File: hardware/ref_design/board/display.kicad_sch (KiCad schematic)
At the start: 13 parts, among them J3 FH35C-39S-0.3SHW(50), U6 TPS61160DRVR

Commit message: Reference design: case, board pipeline, routing tools and docs
- case/case.scad now owns every position the board needs (outline,
  cable slot, contacts, screws, USB-C, power button, pinholes, light
  pipes, height limits) and exports them to positions.json; tub, lid
  and power cap STLs, lens and board outlines as DXF.
- board/placement.py + tools/build_pcb.py: a 4-layer board built from
  KiCad's netlist with pcbnew, every footprint linked to its symbol
  (DRC schematic parity: 0), the RP2350B core's placement, routing and
  regulator copper copied from Raspberry Pi's minimal design.
- tools/route.py: planes, pre-routes the autorouter can't do (membrane
  combs, the display's grounded RGB pins, plane fan-out), Freerouting
  1.9 on a corrected copy of the board, pours, stitching, repair.
- Footprint copies that carry vendor 3D models (USB-C, JST, switches)
  checked against their pads; speaker pads moved to the back as SMD;
  the Alps switch's pads pulled back from its locating holes.
- docs: README, assembly, bring-up, pin map (generated), BOM, design
  review, and the Konnect problems met on the way.

Co-Authored-By: Claude Opus 5.5 (1M context) <noreply@anthropic.com>
Claude-Session: https://claude.ai/code/session_01KGgEu3CbFtCsvHRQgAFiCN
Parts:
- U6: footprint Package_SON:WSON-6-1EP_2x2mm_P0.65mm_EP1x1.6mm -> Package_SON:WSON-6-1EP_2x2mm_P0.65mm_EP1x1.6mm_ThermalVias
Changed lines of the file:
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@@
         (font
           (size 1.27 1.27))))
-    (property "Footprint" "Package_SON:WSON-6-1EP_2x2mm_P0.65mm_EP1x1.6mm"
+    (property "Footprint" "Package_SON:WSON-6-1EP_2x2mm_P0.65mm_EP1x1.6mm_ThermalVias"
       (at 137.16 88.9 0)
       (effects

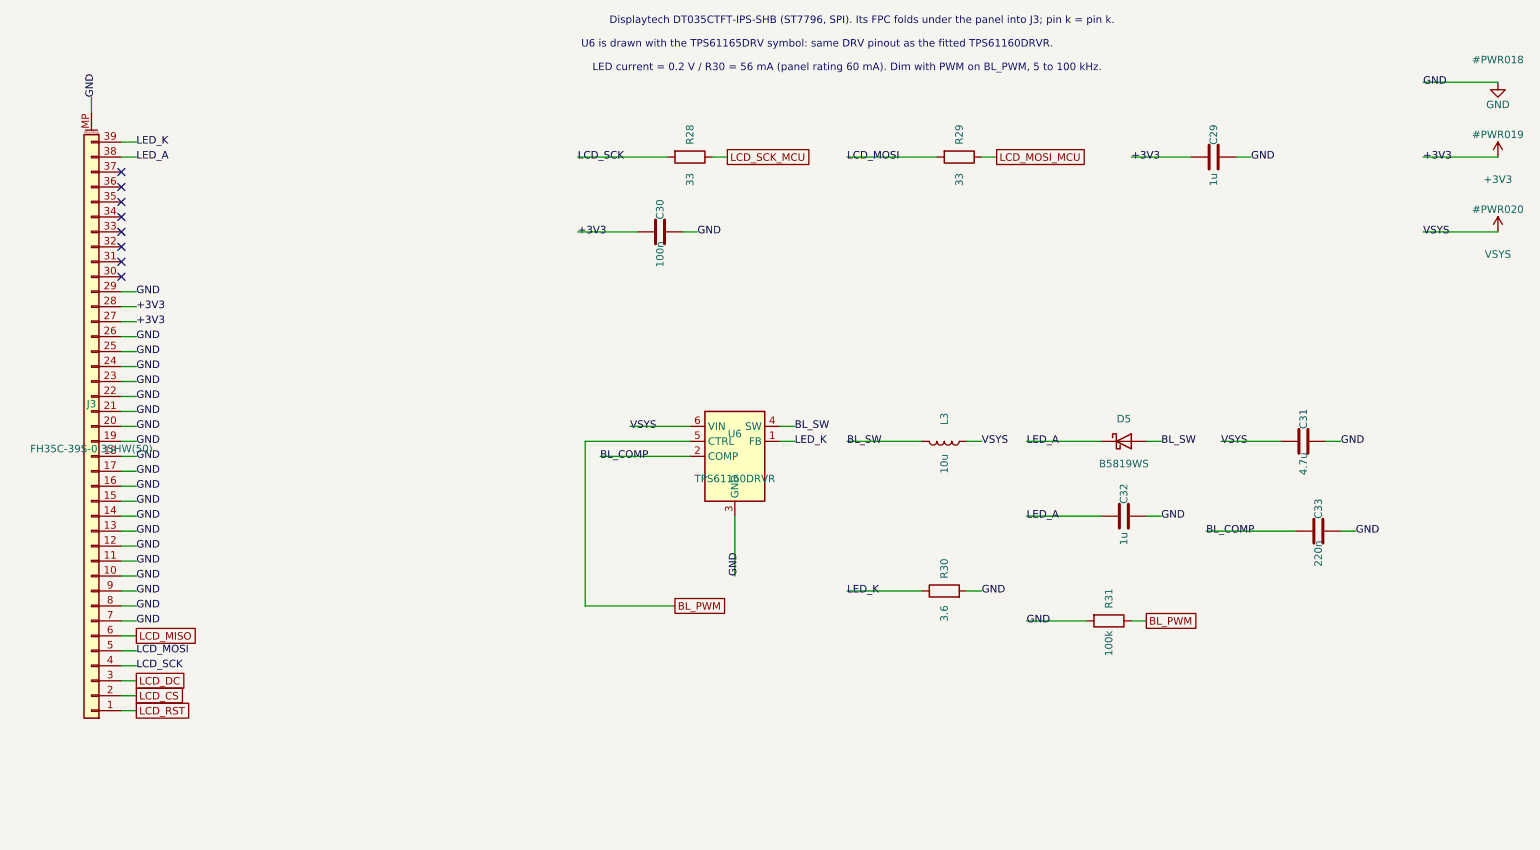
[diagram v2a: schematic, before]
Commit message: Reference design: QD3525 panel, fab outputs, fit check
The $25-35 Displaytech DT035 is replaced by the QD3525, a bare 3.5in IPS
ST7796U panel of the same class at about $5-8 with a published drawing
and pinout (the panel inside LCDwiki's MSP3525 module).

- J3 is now the landing for its 48-contact solder tail (tools/fp_panel.py),
  wired as the maker's module wires it; TE goes to GPIO32.
- Backlight: an AP3156 charge pump drives each of the six parallel LEDs
  through its own current sink, set over one GPIO (BL_SDI). Its symbol
  comes from tools/sym_lib.py (Konnect's create_symbol draws no body).
- case.scad is built around a fixed panel bay, so the board outline,
  buttons and screws stay put; the lid, lens and STLs follow the panel.
- Routing: fan-out vias kept off pads, the AP3156's GND pins stubbed into
  its thermal pad, loose copper trimmed at the end; silk.py re-runnable.
- fab/: gerbers and drill, JLC BOM (40 part numbers) and CPL (91
  placements), STEP, renders, schematic and assembly PDFs.

check_netlist: PASS. ERC: 0 errors. DRC: 0 errors, 0 unconnected,
0 parity issues (2 cosmetic silk warnings at the USB-C). check_fit: PASS.

Co-Authored-By: Claude Opus 5.5 (1M context) <noreply@anthropic.com>
Claude-Session: https://claude.ai/code/session_01KGgEu3CbFtCsvHRQgAFiCN
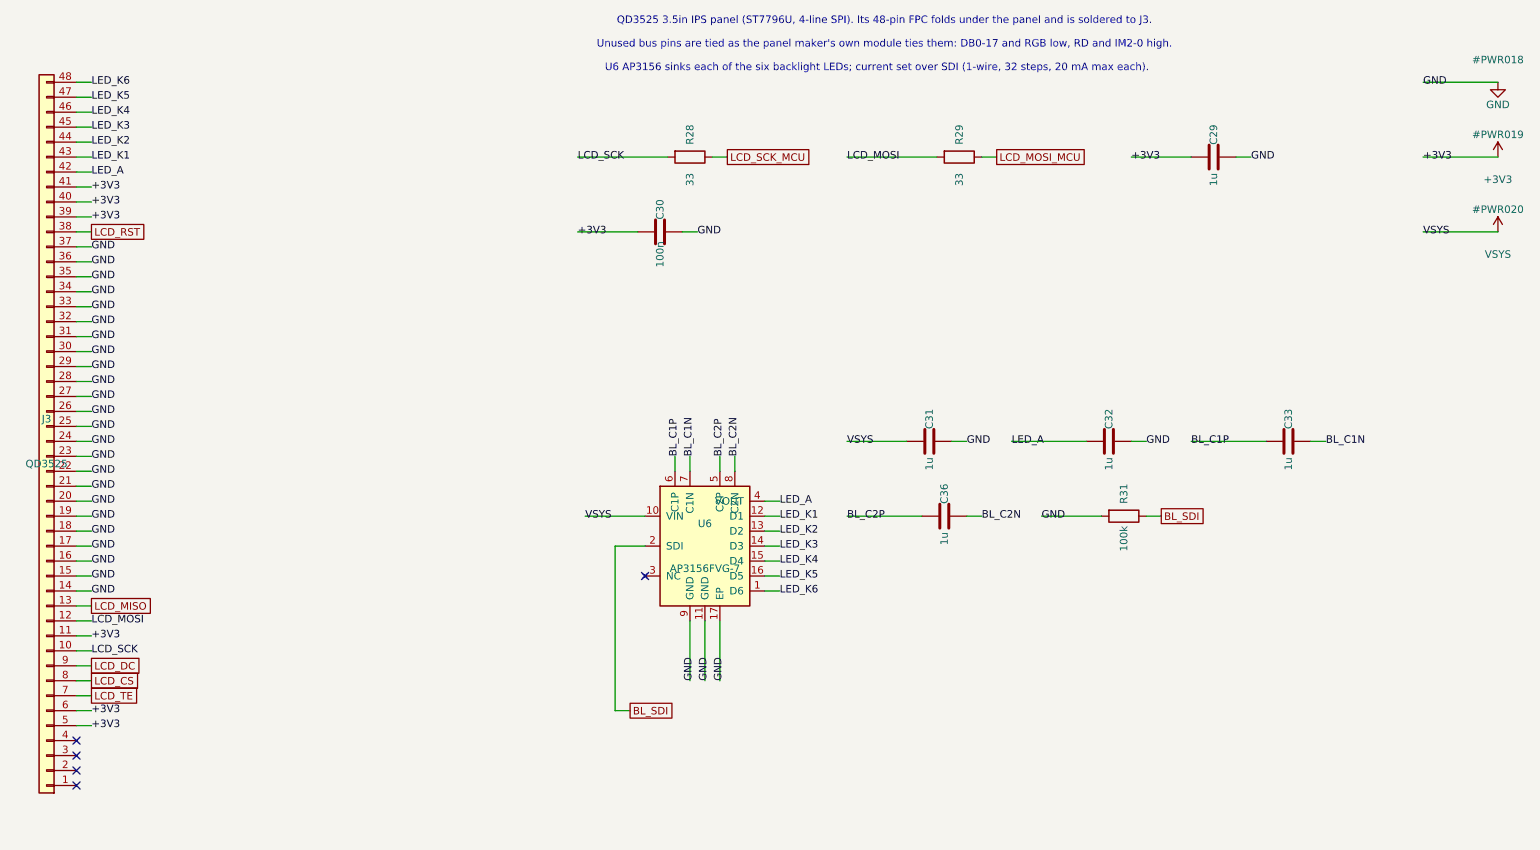
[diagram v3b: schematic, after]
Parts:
- removed D5: B5819WS, Diode_SMD:D_SOD-323, symbol Device:D_Schottky
- removed J3: FH35C-39S-0.3SHW(50), battler:Hirose_FH35C-39S-0.3SHW_1x39-1MP_P0.30mm_Horizontal, symbol Connector_Generic_MountingPin:Conn_01x39_MountingPin
- removed L3: 10u, Inductor_SMD:L_1008_2520Metric, symbol Device:L
- removed R30: 3.6, Resistor_SMD:R_0603_1608Metric, symbol Device:R
- removed U6: TPS61160DRVR, Package_SON:WSON-6-1EP_2x2mm_P0.65mm_EP1x1.6mm_ThermalVias, symbol Driver_LED:TPS61165DRV
- added C36: 1u, Capacitor_SMD:C_0402_1005Metric, symbol Device:C
- added J3: QD3525, battler:QD3525_FPC_1x48_P0.80mm_Solder, symbol Connector_Generic:Conn_01x48
- added U6: AP3156FVG-7, Package_DFN_QFN:QFN-16-1EP_4x4mm_P0.65mm_EP2.5x2.5mm_ThermalVias, symbol battler:AP3156
- C31: value 4.7u -> 1u; footprint Capacitor_SMD:C_0603_1608Metric -> Capacitor_SMD:C_0402_1005Metric; LCSC C19666 -> C52923; MPN CL10A475KO8NNNC -> CL05A105KA5NQNC
- C32: footprint Capacitor_SMD:C_0603_1608Metric -> Capacitor_SMD:C_0402_1005Metric; LCSC C15849 -> C52923; MPN CL10A105KB8NNNC -> CL05A105KA5NQNC
- C33: value 220n -> 1u; LCSC C16772 -> C52923; MPN CL05B224KO5NNNC -> CL05A105KA5NQNC
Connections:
- net +3V3: now also J3.11 (Pin_11), J3.39 (Pin_39), J3.40 (Pin_40), J3.41 (Pin_41), J3.5 (Pin_5), J3.6 (Pin_6)
- net GND: now also J3.14 (Pin_14), J3.15 (Pin_15), J3.16 (Pin_16), J3.17 (Pin_17), J3.18 (Pin_18), J3.19 (Pin_19), J3.20 (Pin_20), J3.21 (Pin_21), J3.22 (Pin_22), J3.23 (Pin_23), J3.24 (Pin_24), J3.25 (Pin_25), J3.26 (Pin_26), J3.27 (Pin_27), J3.28 (Pin_28), J3.29 (Pin_29), J3.30 (Pin_30), J3.31 (Pin_31), J3.32 (Pin_32), J3.33 (Pin_33), J3.34 (Pin_34), J3.35 (Pin_35), J3.36 (Pin_36), J3.37 (Pin_37), U6.11 (GND), U6.17 (EP), U6.9 (GND); no longer C33.2
- net LCD_CS: now also J3.8 (Pin_8)
- net LCD_DC: now also J3.9 (Pin_9)
- net LCD_MISO: now also J3.13 (Pin_13)
- net LCD_MOSI: now also J3.12 (Pin_12)
- net LCD_RST: now also J3.38 (Pin_38)
- net LCD_SCK: now also J3.10 (Pin_10)
- net LED_A: now also J3.42 (Pin_42), U6.4 (VOUT)
- net VSYS: now also U6.10 (VIN)
- net BL_COMP renamed BL_C1P
- net BL_C1P: now also U6.6 (C1P)
- net BL_PWM renamed BL_SDI
- net BL_SDI: now also U6.2 (SDI)
- new net BL_C1N: C33.2, U6.7 (C1N)
- new net BL_C2N: C36.2, U6.8 (C2N)
- new net BL_C2P: C36.1, U6.5 (C2P)
- new net LCD_TE: J3.7 (Pin_7)
- new net LED_K1: J3.43 (Pin_43), U6.12 (D1)
- new net LED_K2: J3.44 (Pin_44), U6.13 (D2)
- new net LED_K3: J3.45 (Pin_45), U6.14 (D3)
- new net LED_K4: J3.46 (Pin_46), U6.15 (D4)
- new net LED_K5: J3.47 (Pin_47), U6.16 (D5)
- new net LED_K6: J3.48 (Pin_48), U6.1 (D6)
- no-connect marks 8 -> 5
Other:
- note added: "QD3525 3.5in IPS panel (ST7796U, 4-line SPI). Its 48-pin FPC folds under the panel and is soldered to J3."
- note added: "U6 AP3156 sinks each of the six backlight LEDs; current set over SDI (1-wire, 32 steps, 20 mA max each)."
- note added: "Unused bus pins are tied as the panel maker's own module ties them: DB0-17 and RGB low, RD and IM2-0 high."
- note removed: "Displaytech DT035CTFT-IPS-SHB (ST7796, SPI). Its FPC folds under the panel into J3; pin k = pin k."
- note removed: "LED current = 0.2 V / R30 = 56 mA (panel rating 60 mA). Dim with PWM on BL_PWM, 5 to 100 kHz."
- note removed: "U6 is drawn with the TPS61165DRV symbol: same DRV pinout as the fitted TPS61160DRVR."

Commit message: Reference design: plug-in ER-TFT035IPS-6 panel, pins and pin escapes for 2 layers
- Panel: EastRising ER-TFT035IPS-6 (ILI9488, 320x480 IPS) on a Hirose FH12-50S
  ZIF connector (J3) that JLC places, instead of the QD3525's hand-soldered tail.
  Case panel/FPC geometry, fit check (FPC zones), backlight sinks paired onto
  its two cathode pins, docs and BOM updated. Prices from both shops' carts:
  about $14.20 a unit at 10 with shipping.
- Pins reassigned for two layers: each faces where its net goes, in fan-out
  order (seat 1's face buttons, panel reset, backlight and ADC inputs on
  GPIO40-47; seat 1's cross and the panel's TE on GPIO28-32).
- build_pcb.copy_escapes: Raspberry Pi's own routing out of the RP2354B's pins,
  copied with the core and locked, so no pin gets boxed in by its neighbours.
  The board now routes completely in about 10 minutes.
- route.py: loose tracks are trimmed back to their last real join instead of
  deleted (Freerouting meets stubs part-way along), T-joins are split and
  duplicate tracks dropped; Freerouting routes to +5 um clearance and a 0.12 mm
  inset outline (it rounded under 0.15 mm and hugged the board edge).
- MCU sheet region widened for the longer labels; datasheet list updated for
  the 2-layer parts; old panel landing footprint/tool and the unused side
  switch footprint removed.

Checks: netlist PASS (122 parts, 115 nets), ERC 0, DRC 0 errors / 0
unconnected / 0 parity (2 cosmetic silk warnings), holes 0.3/0.6/0.65/2.2 mm,
fit PASS on 91 parts.

Co-Authored-By: Claude Opus 5.5 <noreply@anthropic.com>
Claude-Session: https://claude.ai/code/session_01KGgEu3CbFtCsvHRQgAFiCN
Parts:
- removed J3: QD3525, battler:QD3525_FPC_1x48_P0.80mm_Solder, symbol Connector_Generic:Conn_01x48
- added J3: FH12-50S-0.5SH(55), Connector_FFC-FPC:Hirose_FH12-50S-0.5SH_1x50-1MP_P0.50mm_Horizontal, symbol Connector_Generic_MountingPin:Conn_01x50_MountingPin
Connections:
- net LED_K3 is gone; now on net LED_K1: U6.14 (D3)
- net LED_K4 is gone; now on net LED_K2: U6.15 (D4)
- net LED_K5 is gone; now on net LED_K2: U6.16 (D5)
- net LED_K6 is gone; now on net LED_K2: U6.1 (D6)
- net +3V3: now also J3.10 (Pin_10), J3.11 (Pin_11), J3.16 (Pin_16), J3.42 (Pin_42), J3.43 (Pin_43), J3.44 (Pin_44), J3.9 (Pin_9)
- net GND: now also J3.1 (Pin_1), J3.19 (Pin_19), J3.2 (Pin_2), J3.20 (Pin_20), J3.21 (Pin_21), J3.22 (Pin_22), J3.23 (Pin_23), J3.24 (Pin_24), J3.25 (Pin_25), J3.26 (Pin_26), J3.27 (Pin_27), J3.28 (Pin_28), J3.29 (Pin_29), J3.3 (Pin_3), J3.30 (Pin_30), J3.31 (Pin_31), J3.32 (Pin_32), J3.33 (Pin_33), J3.34 (Pin_34), J3.35 (Pin_35), J3.36 (Pin_36), J3.37 (Pin_37), J3.38 (Pin_38), J3.39 (Pin_39), J3.40 (Pin_40), J3.8 (Pin_8)
- net LCD_CS: now also J3.13 (Pin_13)
- net LCD_DC: now also J3.14 (Pin_14)
- net LCD_MISO: now also J3.18 (Pin_18)
- net LCD_MOSI: now also J3.17 (Pin_17)
- net LCD_RST: now also J3.41 (Pin_41)
- net LCD_SCK: now also J3.15 (Pin_15)
- net LCD_TE: now also J3.12 (Pin_12)
- net LED_A: now also J3.50 (Pin_50)
- net LED_K1: now also U6.13 (D2), J3.49 (Pin_49)
- net LED_K2: now also J3.48 (Pin_48); no longer U6.13 (D2)
- no-connect marks 5 -> 9
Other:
- note added: "EastRising ER-TFT035IPS-6 (ILI9488, 4-wire SPI). Its 50-pin FPC folds under the panel into J3 (ZIF)."
- note added: "J3 pin j is panel pin 51 - j. Unused bus pins as the datasheet says: DB0-17 and RGB low, RD and IM2-0 high."
- note added: "U6 AP3156: three sinks per cathode pin (LED_K1, LED_K2), 20 mA per LED at most, set over SDI (1-wire)."
- note removed: "QD3525 3.5in IPS panel (ST7796U, 4-line SPI). Its 48-pin FPC folds under the panel and is soldered to J3."
- note removed: "U6 AP3156 sinks each of the six backlight LEDs; current set over SDI (1-wire, 32 steps, 20 mA max each)."
- note removed: "Unused bus pins are tied as the panel maker's own module ties them: DB0-17 and RGB low, RD and IM2-0 high."
